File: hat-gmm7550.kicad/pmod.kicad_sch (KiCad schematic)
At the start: 19 parts, among them J10 Pmod 2x6, J7 10144517-064802LF, J9 Pmod 2x6, U4 LSF0204PW, U5 LSF0204PW, U6 LSF0204PW, U7 LSF0204PW

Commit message: Update copyright years and increment revision
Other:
- note added: "Copyright (c) 2022-2024 Anton Kuzmin Licensed under CERN-OHL-P v2 https://github.com/gmm-7550/"
- note removed: "Copyright (c) 2022 Anton Kuzmin Licensed under CERN-OHL-P v2 https://github.com/ak-fau/gmm7550.git"
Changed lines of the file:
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@@
   (title_block
     (title "40-pin GPIO HAT adapter for GMM-7550")
-    (date "2022-04-24")
-    (rev "1.1")
+    (date "2024-01-27")
+    (rev "1.2")
   )
   (junction (at 120.65 45.72) (diameter 0) (color 0 0 0 0)
@@
     (stroke (width 0) (type default))
   )
-  (text "Copyright (c) 2022  Anton Kuzmin\nLicensed under CERN-OHL-P v2\nhttps://github.com/ak-fau/gmm7550.git"
+  (text "Copyright (c) 2022-2024  Anton Kuzmin\nLicensed under CERN-OHL-P v2\nhttps://github.com/gmm-7550/"
     (at 198.12 179.07 0)
     (effects (font (size 2.54 2.54)) (justify left bottom))

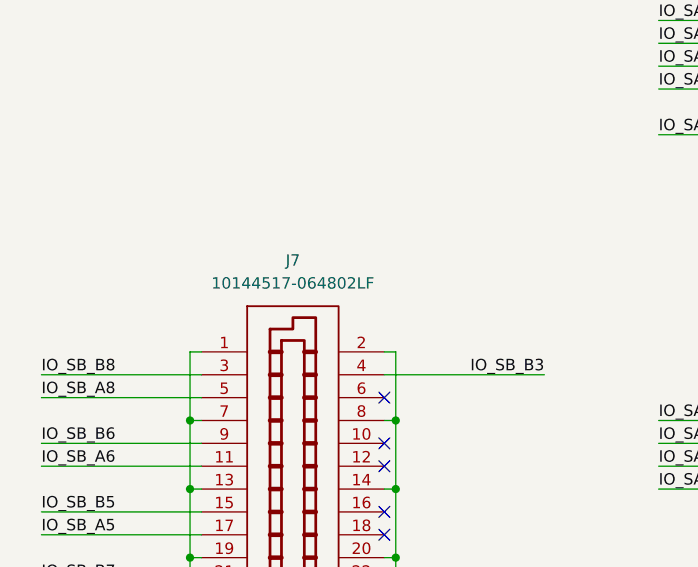
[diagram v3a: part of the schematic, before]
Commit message: Change module connector part number: 9mm board-to-board distance
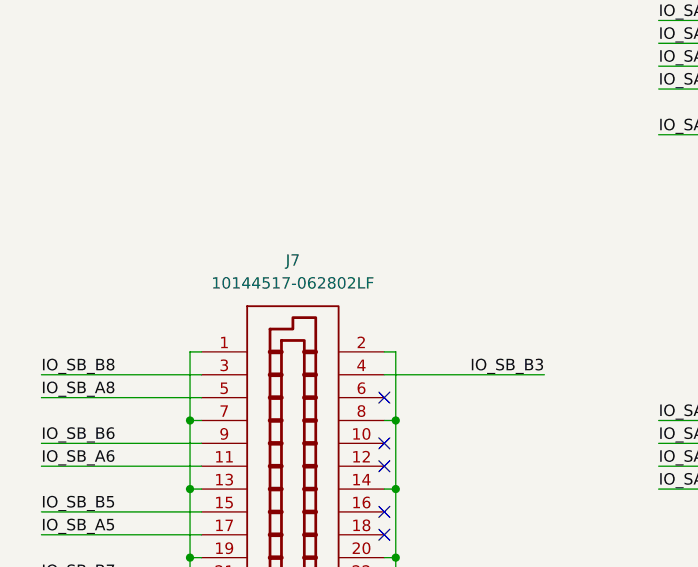
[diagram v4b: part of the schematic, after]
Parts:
- J7: value 10144517-064802LF -> 10144517-062802LF
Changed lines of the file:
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@@
       (effects (font (size 1.27 1.27)))
     )
-    (property "Value" "10144517-064802LF" (at 62.23 62.23 0)
+    (property "Value" "10144517-062802LF" (at 62.23 62.23 0)
       (effects (font (size 1.27 1.27)))
     )
